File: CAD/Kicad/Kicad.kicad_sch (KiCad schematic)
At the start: 37 parts, among them J1 USB_C_Receptacle_USB2.0_14P, J2 USB_C_Receptacle_USB2.0_14P, J3 Conn_01x20_Pin, J4 Conn_01x20_Pin, Q1 2N3904, Q2 2N3904, SW1 SW_Push, SW2 SW_Push, U1 ESP32-S3-WROOM-2, U3 AMS1117-3.3, U7 BME680, U8 MPU-9250, U9 FT231XQ

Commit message: Finalized this project
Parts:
- removed C7, C8: 0.1uF, Capacitor_SMD:C_0805_2012Metric, symbol Device:C
- removed D1, D2, D3, D4: D_Schottky, Diode_SMD:D_SOD-123, symbol Device:D_Schottky
- removed FB1, FB2: FerriteBead, Inductor_SMD:L_0805_2012Metric_Pad1.05x1.20mm_HandSolder, symbol Device:FerriteBead
- removed J2: USB_C_Receptacle_USB2.0_14P, Connector_USB:USB_C_Receptacle_Amphenol_12401610E4-2A, symbol Connector:USB_C_Receptacle_USB2.0_14P
- removed J3, J4: Conn_01x20_Pin, Connector_PinHeader_2.54mm:PinHeader_1x20_P2.54mm_Vertical, symbol Connector:Conn_01x20_Pin
- removed R10, R11: 5K1, Resistor_SMD:R_0603_1608Metric_Pad0.98x0.95mm_HandSolder, symbol Device:R
- removed U3: AMS1117-3.3, Package_TO_SOT_SMD:SOT-223-3_TabPin2, symbol Regulator_Linear:AMS1117-3.3
- removed U7: BME680, Package_LGA:Bosch_LGA-8_3x3mm_P0.8mm_ClockwisePinNumbering, symbol Sensor:BME680
- added C12: 22uF, Capacitor_SMD:C_01005_0402Metric, symbol Device:C
- added C13, C15, C16, C18: 10uF, Capacitor_SMD:C_01005_0402Metric, symbol Device:C
- added C14, C20: 0.1uF, Capacitor_SMD:C_01005_0402Metric, symbol Device:C
- added C5, C6: 1uF, Capacitor_SMD:C_01005_0402Metric, symbol Device:C
- added R16, R17: 470R, Resistor_SMD:R_0201_0603Metric, symbol Device:R
- added U2: TLV75533PDRV, Package_SON:WSON-6-1EP_2x2mm_P0.65mm_EP1x1.6mm, symbol Regulator_Linear:TLV75533PDRV
- C10, C3, C4, C9: footprint Capacitor_SMD:C_0805_2012Metric -> Capacitor_SMD:C_01005_0402Metric
- C11: footprint Capacitor_SMD:C_0805_2012Metric -> Capacitor_SMD:C_0201_0603Metric
- J1: footprint Connector_USB:USB_C_Receptacle_Amphenol_12401610E4-2A -> Connector_USB:USB_C_Receptacle_G-Switch_GT-USB-7025; Field5 (none) -> C2927036
- Q1, Q2: footprint Package_TO_SOT_THT:TO-92S -> Package_TO_SOT_THT:TO-92Flat
- R1, R2, R3, R4, R5, R6, R7, R8, R9: footprint Resistor_SMD:R_0603_1608Metric_Pad0.98x0.95mm_HandSolder -> Resistor_SMD:R_0201_0603Metric
- SW1, SW2: footprint Button_Switch_SMD:SW_SPST_EVQP2_MiddlePushTravel_H2.5mm -> Button_Switch_SMD:SW_SPST_B3U-1000P
- U1: LCSC Part # (none) -> C42417293
- U8: Field5 (none) -> C71459
- U9: Field5 (none) -> C132159
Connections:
- net 5V_USB_1: now also C5.1, U2.4 (EN), U2.6 (IN)
- net GND: now also C10.1, C3.1, C9.2, R2.2, C12.2, C13.2, C14.1, C15.2, C16.2, C18.2, C20.1, C5.2, C6.2, U2.3 (GND), U2.7 (GND)
- net VCC0: now also C10.2, U8.13 (VDD), U8.8 (VDDIO), C12.1, C13.1, C14.2, C15.1, C16.1, C18.1, C20.2, C6.1, U2.1 (OUT); no longer C10.1, C3.1
- net ESP32_RXD renamed ESP32_SERIAL_N
- net ESP32_SERIAL_N: now also R17.1, R17.2
- net ESP32_TXD renamed ESP32_SERIAL_P
- net ESP32_SERIAL_P: now also R16.1, R16.2
- net NATIVE_D+: no longer names the net of U1.14 (USB_D+/IO20)
- net NATIVE_D-: no longer names the net of U1.13 (USB_D-/IO19)
- no-connect marks 12 -> 13
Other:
- note added: "BLOCK DIAGRAM"
- note added: "ESP32-S3-WROOM-2"
- note removed: "Env sensor"
- note removed: "GPIO Header"
- note removed: "Power ORing"
- note removed: "Serial USB"
- moved on the sheet: C10, C11, C3, C4, C9, J1, Q1, Q2, R1, R2, R3, R4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

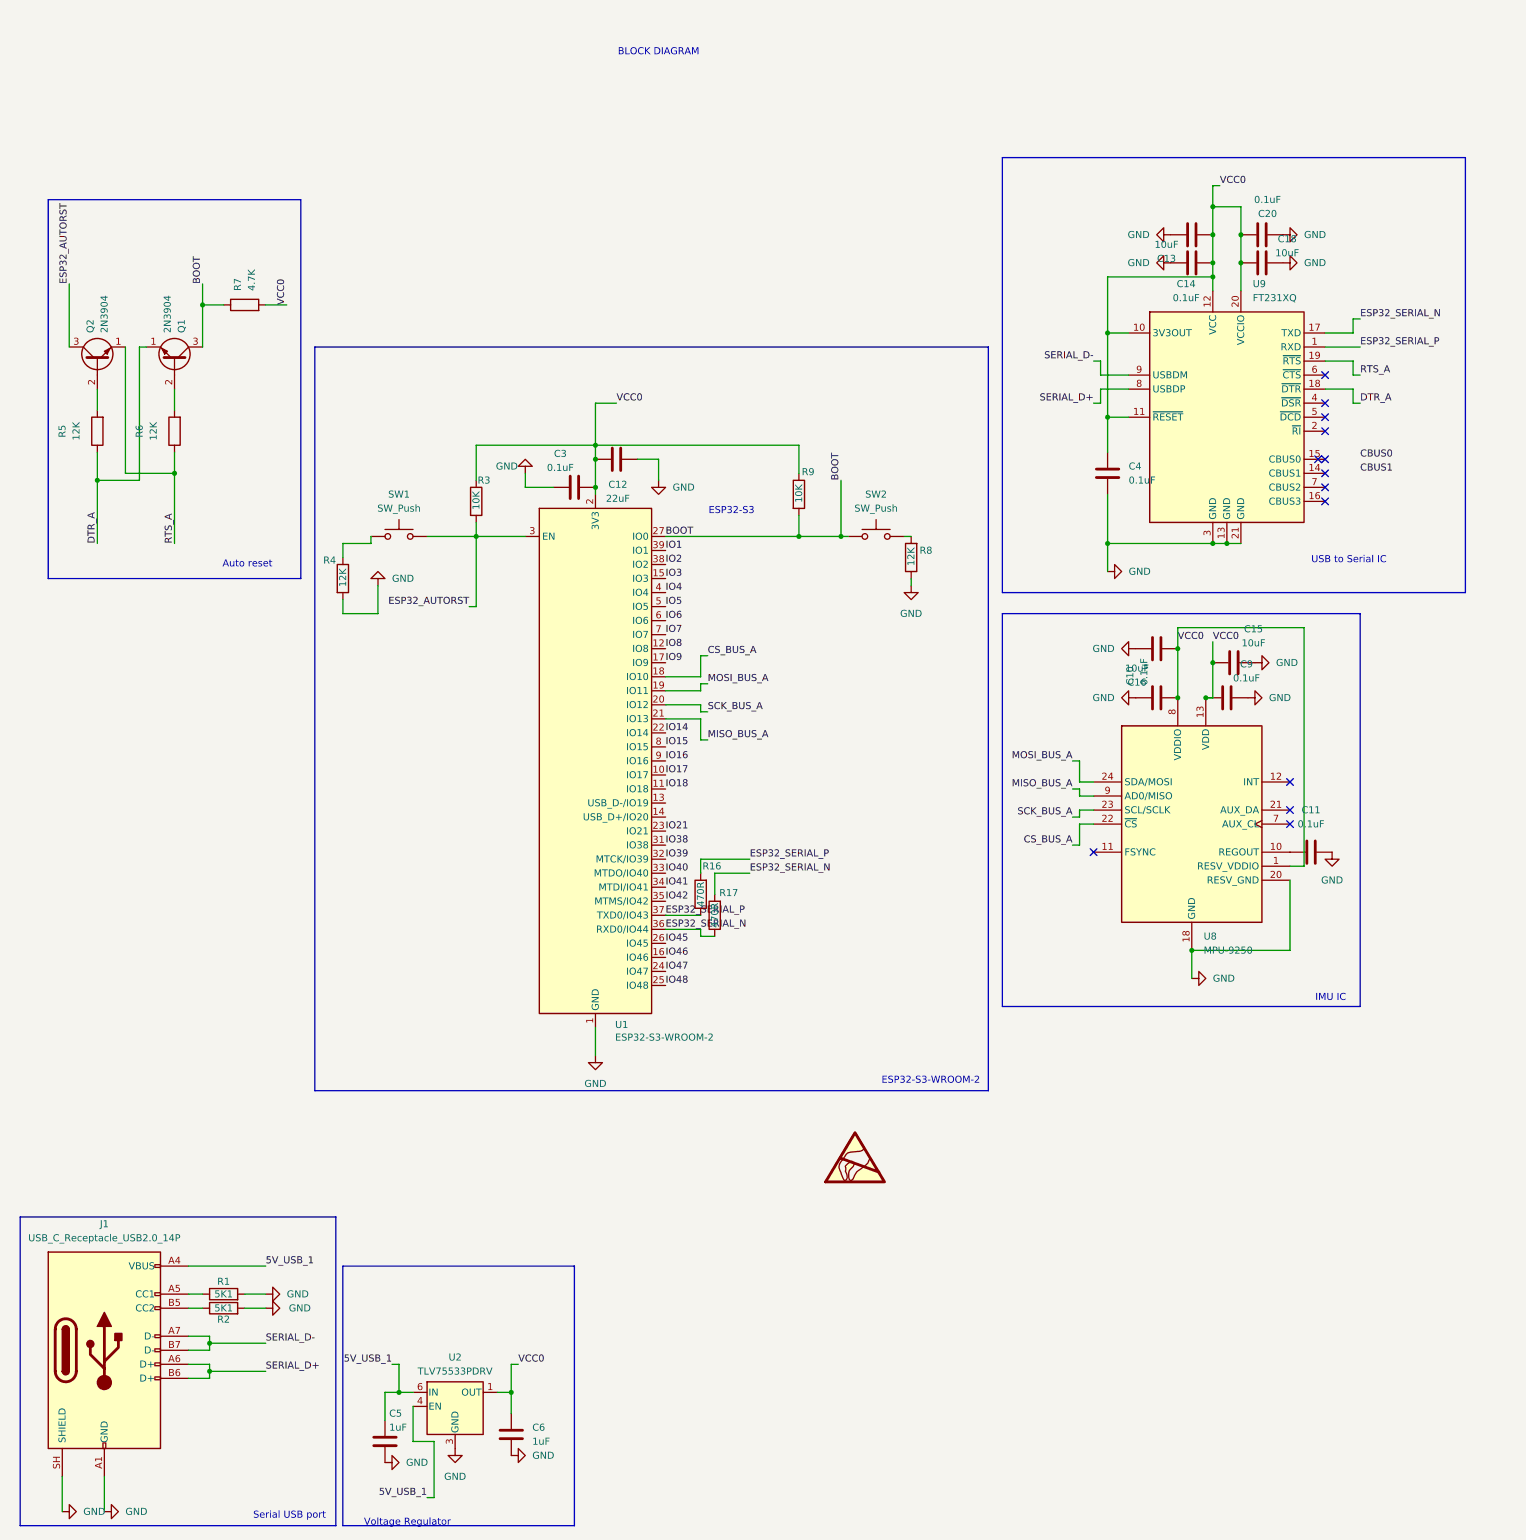
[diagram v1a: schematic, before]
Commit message: Generated a BOM and organized the entire Repo
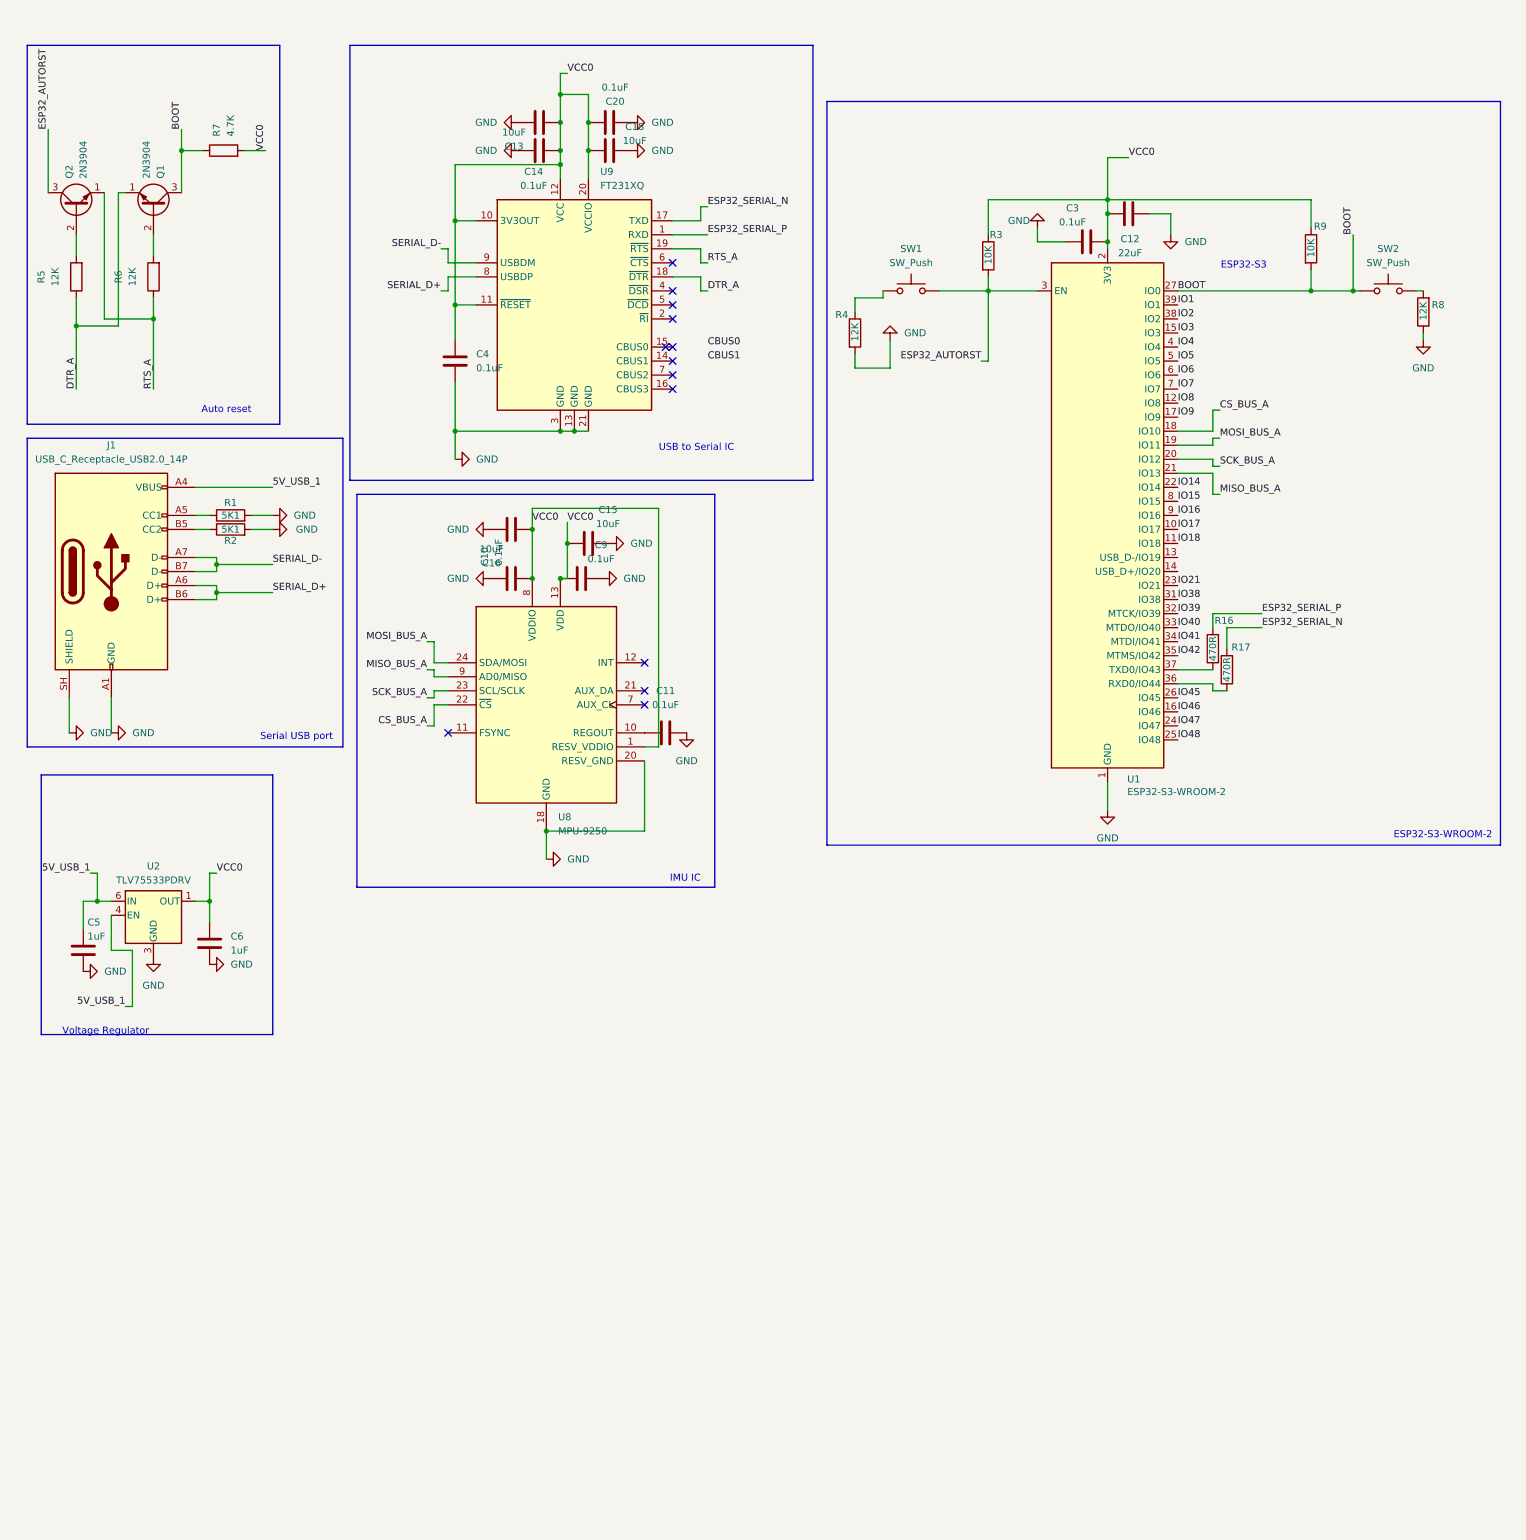
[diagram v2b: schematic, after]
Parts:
- C10, C11, C14, C20, C3, C4, C9: LCSC Part # (none) -> C1525
- C12: LCSC Part # (none) -> C105226
- C13, C15, C16, C18: LCSC Part # (none) -> C15525
- C5, C6: LCSC Part # (none) -> C14445
- J1: Field5 C2927036 -> (none); LCSC Part # (none) -> C963213
- Q1, Q2: C118538 (none) -> C118538
- R1, R2: LCSC Part # (none) -> C177348
- R16, R17: LCSC Part # (none) -> C177340
- R3, R9: LCSC Part # (none) -> C177337
- R4, R5, R6, R8: LCSC Part # (none) -> C177293
- R7: LCSC Part # (none) -> C22356632
- SW1, SW2: LCSC Part # (none) -> C231329
- U2: Field5 C2861750 -> (none); LCSC Part # (none) -> C2861750
- U8: Field5 C71459 -> (none); LCSC Part # (none) -> C71459
- U9: Field5 C132159 -> (none); LCSC Part # (none) -> C132159
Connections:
- net ESP32_SERIAL_N: no longer R17.1, U1.36 (RXD0/IO44)
- net ESP32_SERIAL_P: no longer R16.1, U1.37 (TXD0/IO43)
- new net: R17.1, U1.36 (RXD0/IO44)
- new net: R16.1, U1.37 (TXD0/IO43)
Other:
- note removed: "BLOCK DIAGRAM"
- moved on the sheet: C10, C11, C12, C13, C14, C15, C16, C18, C20, C3, C4, C5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
